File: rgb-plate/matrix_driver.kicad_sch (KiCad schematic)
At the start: 0 parts

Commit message: added additional sheets and leds with matrix driver and first regulator
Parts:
- added R1: R, symbol Device:R
- added R2: 10k, symbol Device:R
- added U1: LP5891MRRFR, VQFN76_RRF_TEX, symbol ul_LP5891MRRFR:LP5891MRRFR
- added U2: TPS562202, Package_TO_SOT_SMD:SOT-563, symbol Regulator_Switching:TPS562202
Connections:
- new net: R2.2, U2.5 (EN)
- new net: R1.1, U1.20 (IREF)
- new net +12V: R2.1, U2.1 (VIN)
- new net +3V3: U1.8 (VCC)
- new net B0: U1.3 (B0), U1.6 (B1)
- new net B10: U1.36 (B10)
- new net B12: U1.42 (B12)
- new net B13: U1.45 (B13)
- new net B14: U1.52 (B14)
- new net B15: U1.55 (B15)
- new net B2: U1.13 (B2)
- new net B3: U1.16 (B3)
- new net B4: U1.19 (B4)
- new net B5: U1.23 (B5)
- new net B6: U1.26 (B6)
- new net B7: U1.29 (B7)
- new net B8: U1.30 (B8)
- new net B9: U1.33 (B9)
- new net G0: U1.2 (G0), U1.5 (G1)
- new net G10: U1.37 (G10)
- new net G11: U1.39 (B11), U1.40 (G11)
- new net G12: U1.43 (G12)
- new net G13: U1.46 (G13)
- new net G14: U1.53 (G14)
- new net G15: U1.56 (G15)
- new net G2: U1.12 (G2)
- new net G3: U1.15 (G3)
- new net G4: U1.18 (G4)
- new net G5: U1.22 (G5)
- new net G6: U1.25 (G6)
- new net G7: U1.28 (G7)
- new net G8: U1.31 (G8)
- new net G9: U1.34 (G9)
- new net GND: R1.2, U1.7 (GND), U1.77 (EPAD), U2.3 (GND)
- new net L0: U1.76 (LINE0)
- new net L1: U1.75 (LINE1)
- new net L10: U1.66 (LINE10)
- new net L11: U1.65 (LINE11)
- new net L12: U1.64 (LINE12)
- new net L13: U1.63 (LINE13)
- new net L14: U1.62 (LINE14)
- new net L15: U1.61 (LINE15)
- new net L2: U1.74 (LINE2)
- new net L3: U1.73 (LINE3)
- new net L4: U1.72 (LINE4)
- new net L5: U1.71 (LINE5)
- new net L6: U1.70 (LINE6)
- new net L7: U1.69 (LINE7)
- new net L8: U1.68 (LINE8)
- new net L9: U1.67 (LINE9)
- new net R0: U1.1 (R0), U1.4 (R1)
- new net R10: U1.38 (R10)
- new net R11: U1.41 (R11)
- new net R12: U1.44 (R12)
- new net R13: U1.47 (R13)
- new net R14: U1.54 (R14)
- new net R15: U1.57 (R15)
- new net R2: U1.11 (R2)
- new net R3: U1.14 (R3)
- new net R4: U1.17 (R4)
- new net R5: U1.21 (R5)
- new net R6: U1.24 (R6)
- new net R7: U1.27 (R7)
- new net R8: U1.32 (R8)
- new net R9: U1.35 (R9)

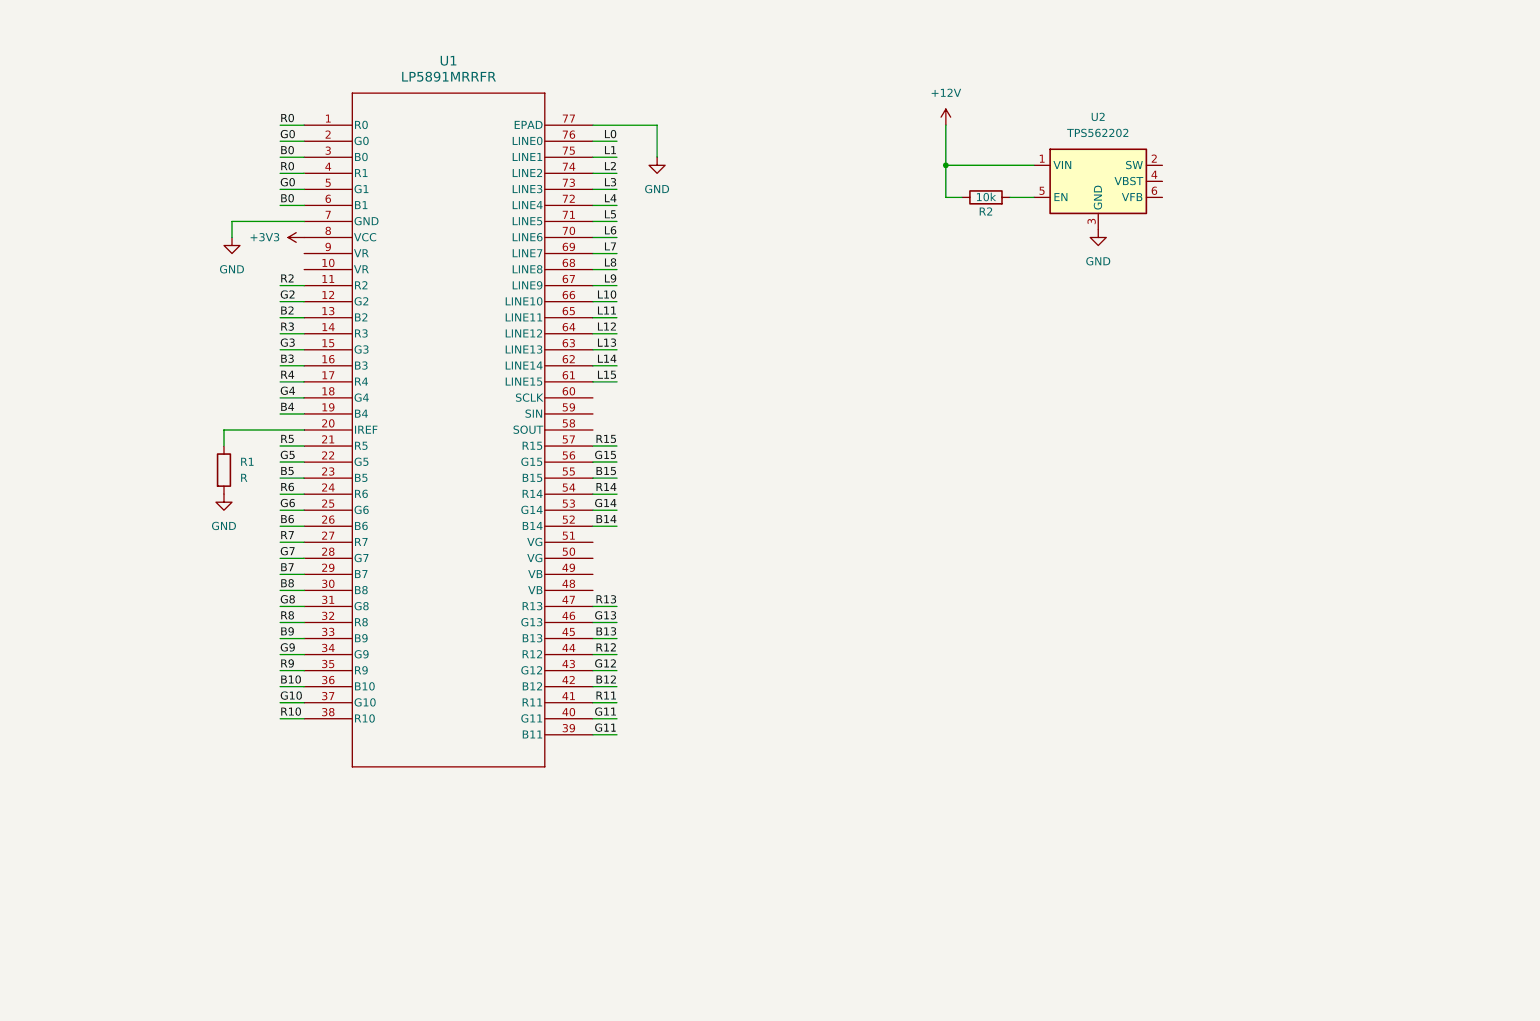
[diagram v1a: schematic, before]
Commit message: added 3 regulators for power stage
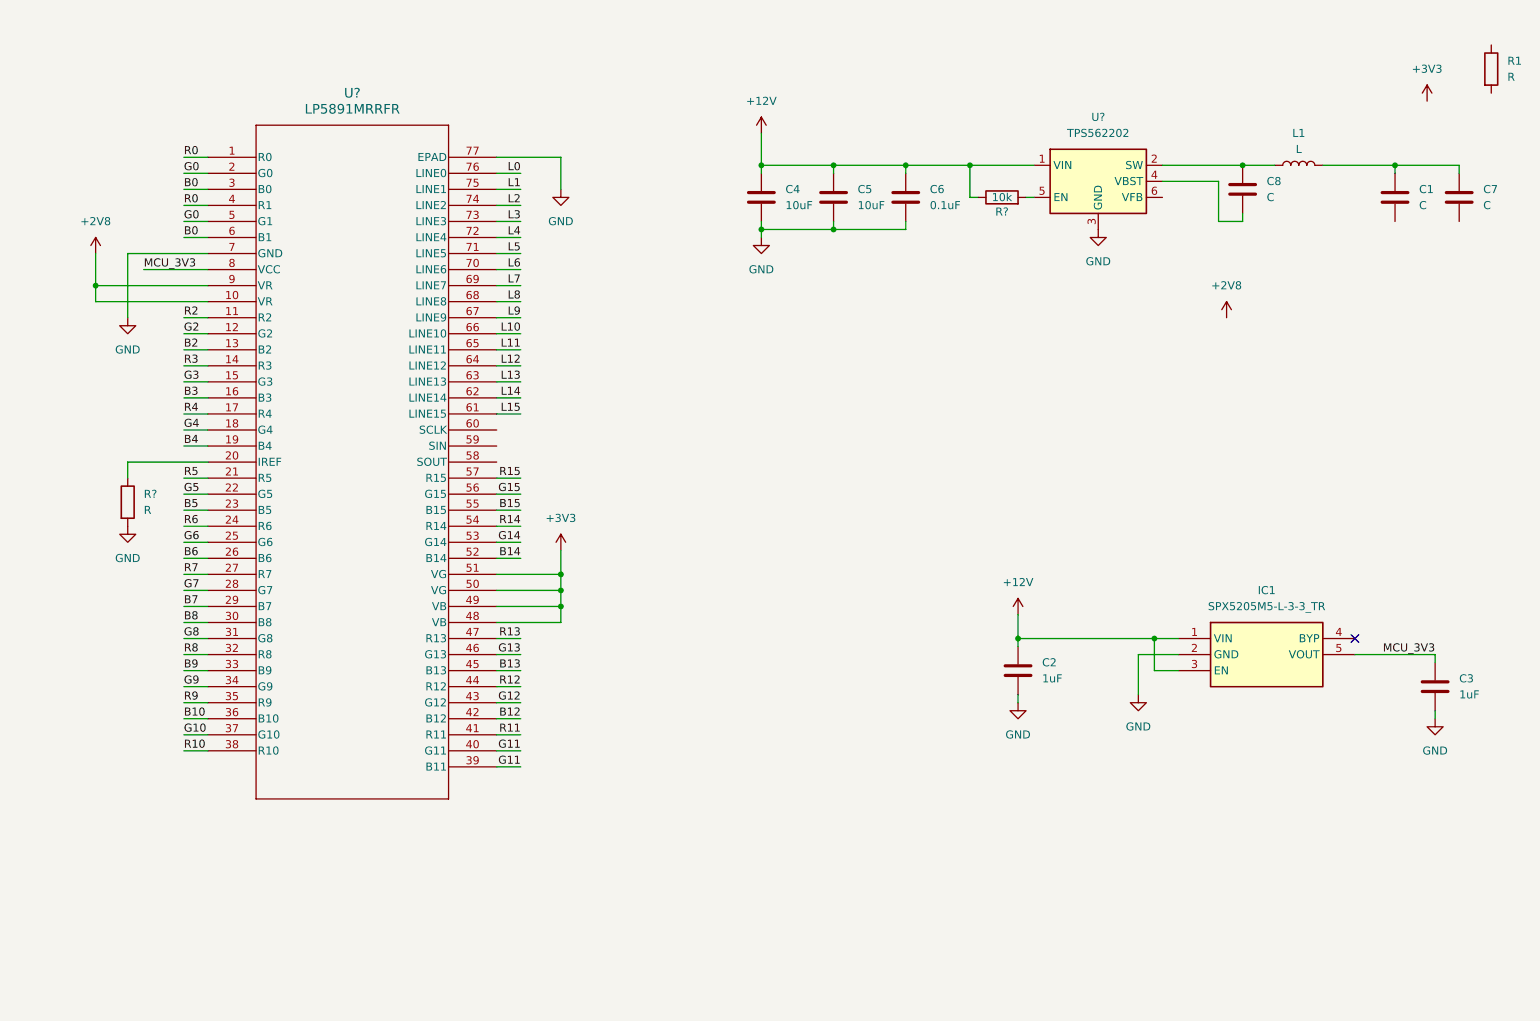
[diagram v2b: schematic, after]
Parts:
- added C1, C7, C8: C, symbol Device:C
- added C2, C3: 1uF, symbol Device:C
- added C4, C5: 10uF, symbol Device:C
- added C6: 0.1uF, symbol Device:C
- added IC1: SPX5205M5-L-3-3_TR, SOT95P280X145-5N, symbol SPX5205M5-L-3-3_TR:SPX5205M5-L-3-3_TR
- added L1: L, symbol Device:L
- added R1: R, symbol Device:R
- renumbered R2 to R?, R1 to R?, U2 to U?, U1 to U?
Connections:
- net +12V: now also C2.1, C4.1, C5.1, C6.1, IC1.1 (VIN), IC1.3 (EN)
- net +3V3: now also U?.48 (VB), U?.49 (VB), U?.50 (VG), U?.51 (VG); no longer U?.8 (VCC)
- net GND: now also C2.2, C3.2, C4.2, C5.2, C6.2, IC1.2 (GND)
- net at U?.2 (SW): now also C8.1, L1.1
- net at U?.4 (VBST): now also C8.2
- net +2V8: now reaches U?.10 (VR)
- net +2V8: now also U?.9 (VR)
- new net: C1.2, C7.2, L1.2
- new net MCU_3V3: C3.1, IC1.5 (VOUT), U?.8 (VCC)
- no-connect marks 0 -> 1
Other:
- moved on the sheet: R?, U?

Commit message: added regulators and components
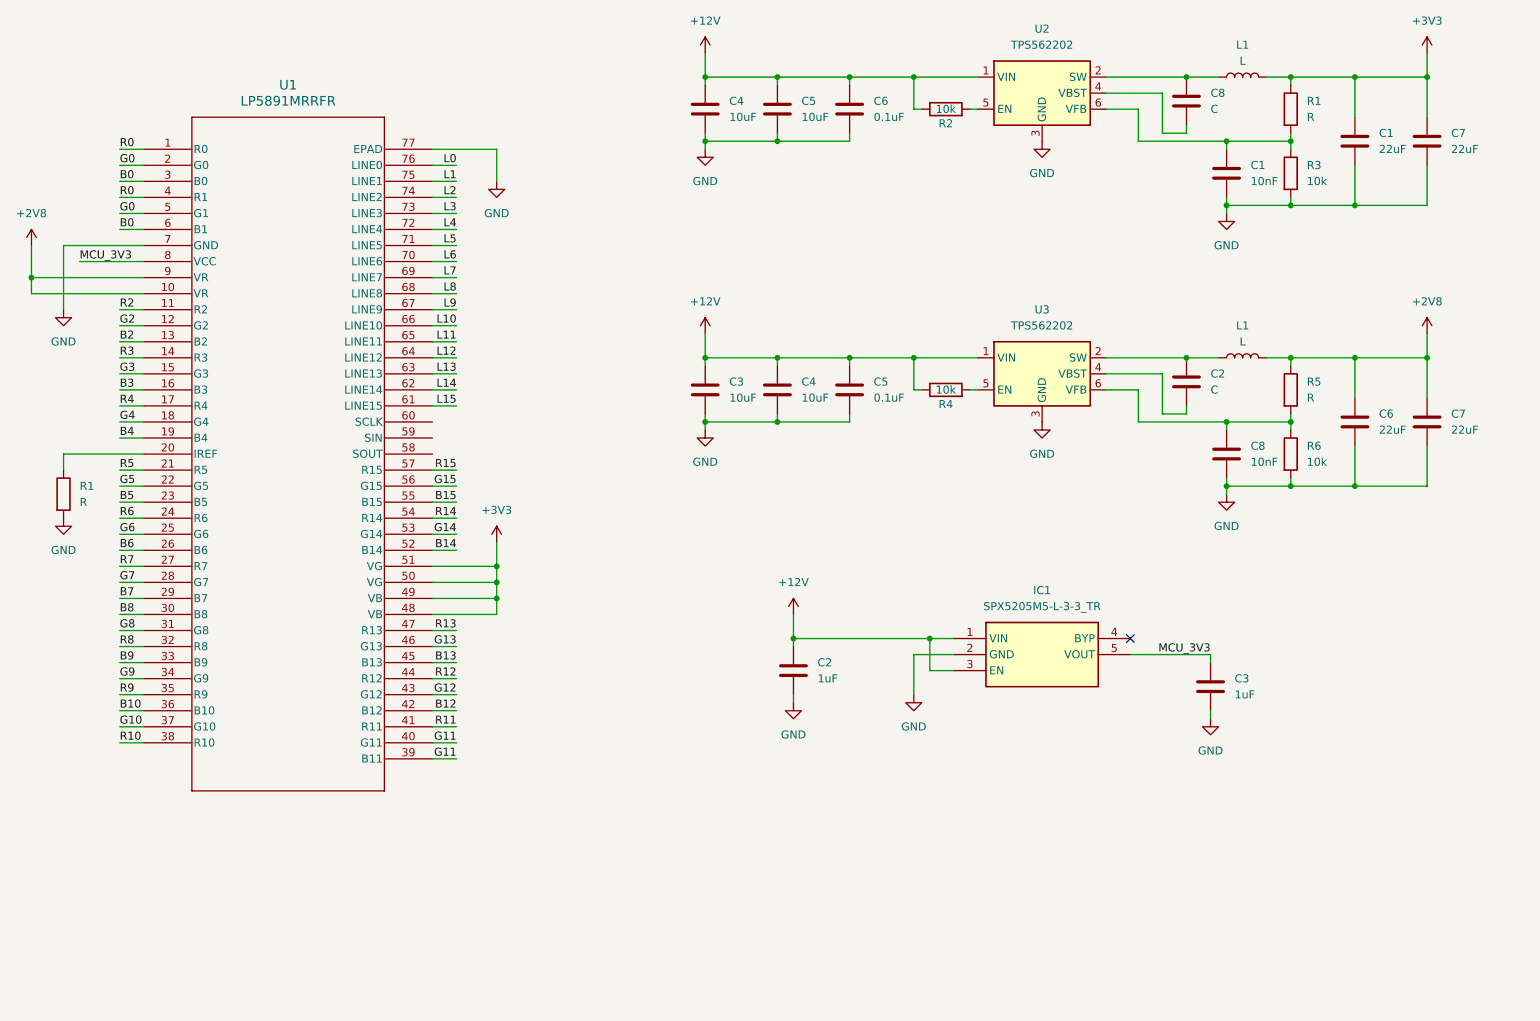
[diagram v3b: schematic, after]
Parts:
- added C1, C8: 10nF, symbol Device:C
- added C2: C, symbol Device:C
- added C3, C4: 10uF, symbol Device:C
- added C5: 0.1uF, symbol Device:C
- added C6, C7: 22uF, symbol Device:C
- added L1: L, symbol Device:L
- added R3, R4, R6: 10k, symbol Device:R
- added R5: R, symbol Device:R
- added U3: TPS562202, Package_TO_SOT_SMD:SOT-563, symbol Regulator_Switching:TPS562202
- C1, C7: value C -> 22uF
- gave numbers to parts that had none: 4
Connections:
- net +12V: now also C3.1, C4.1, C5.1, R4.1, U3.1 (VIN)
- net +2V8: now also C6.2, C7.2, L1.2, R5.1
- net +3V3: now also C1.2, C7.2, L1.2, R1.1
- net GND: now also C1.1, C7.1, C1.1, C3.2, C4.2, C5.2, C6.1, C7.1, C8.1, R3.2, R6.2, U3.3 (GND)
- net at R1.2: now also U2.6 (VFB), C1.2, R3.1
- new net: C8.2, R5.2, R6.1, U3.6 (VFB)
- new net: R4.2, U3.5 (EN)
- new net: C2.1, L1.1, U3.2 (SW)
- new net: C2.2, U3.4 (VBST)
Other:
- moved on the sheet: C1, C2, C3, C4, C5, C6, C7, C8, IC1, L1, R1, R2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

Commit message: initial layout on single board, may need to split up
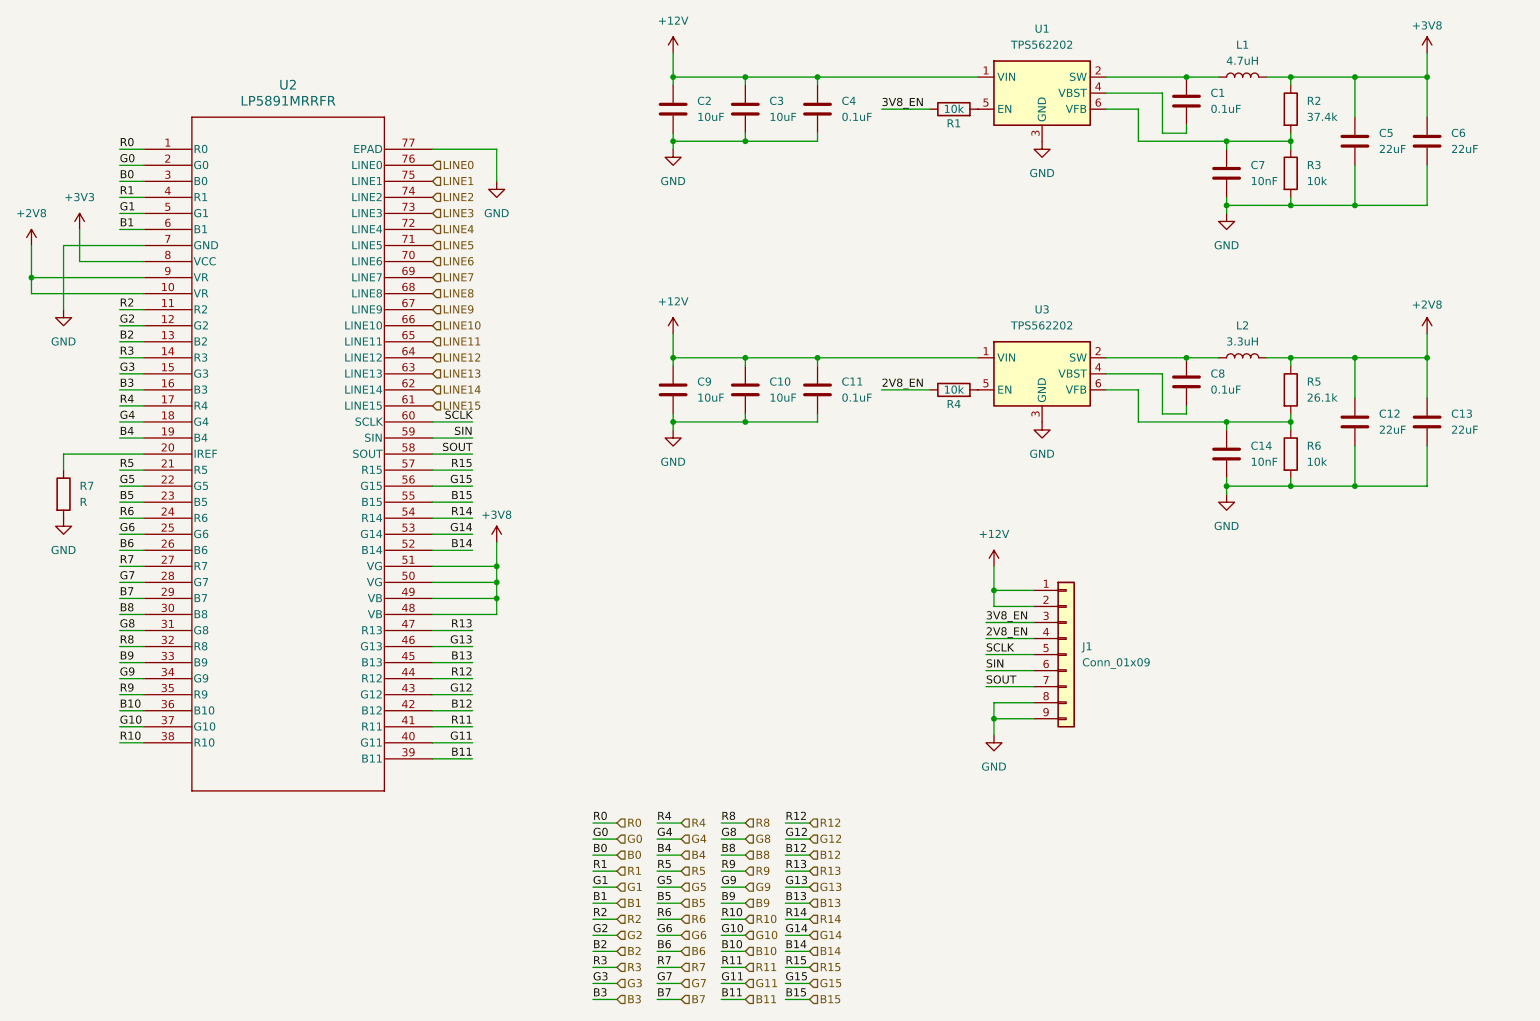
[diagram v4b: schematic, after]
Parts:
- removed C2, C3: 1uF, symbol Device:C
- removed IC1: SPX5205M5-L-3-3_TR, SOT95P280X145-5N, symbol SPX5205M5-L-3-3_TR:SPX5205M5-L-3-3_TR
- added J1: Conn_01x09, symbol Connector_Generic:Conn_01x09
- C1: renamed from C8; value C -> 0.1uF; footprint (none) -> Capacitor_SMD:C_0603_1608Metric
- C10, C2: renamed from C4; footprint (none) -> Capacitor_SMD:C_1206_3216Metric
- C11: renamed from C5; footprint (none) -> Capacitor_SMD:C_0603_1608Metric
- C12: renamed from C6; footprint (none) -> Capacitor_SMD:C_1206_3216Metric
- C13, C6: renamed from C7; footprint (none) -> Capacitor_SMD:C_1206_3216Metric
- C14: renamed from C8; footprint (none) -> Capacitor_SMD:C_0603_1608Metric
- C3: renamed from C5; footprint (none) -> Capacitor_SMD:C_1206_3216Metric
- C4: renamed from C6; footprint (none) -> Capacitor_SMD:C_0603_1608Metric
- C5: renamed from C1; footprint (none) -> Capacitor_SMD:C_1206_3216Metric
- C7: renamed from C1; footprint (none) -> Capacitor_SMD:C_0603_1608Metric
- C8: renamed from C2; value C -> 0.1uF; footprint (none) -> Capacitor_SMD:C_0603_1608Metric
- C9: renamed from C3; footprint (none) -> Capacitor_SMD:C_1206_3216Metric
- L1: value L -> 4.7uH
- L2: renamed from L1; value L -> 3.3uH
- R1: renamed from R2; footprint (none) -> Resistor_SMD:R_0603_1608Metric
- R2: renamed from R1; value R -> 37.4k; footprint (none) -> Resistor_SMD:R_0603_1608Metric
- R3, R4, R6: footprint (none) -> Resistor_SMD:R_0603_1608Metric
- R5: value R -> 26.1k; footprint (none) -> Resistor_SMD:R_0603_1608Metric
- R7: renamed from R1; footprint (none) -> Resistor_SMD:R_0603_1608Metric
- U2: renamed from U1; footprint VQFN76_RRF_TEX -> ul_LP5891MRRFR:VQFN76_RRF_TEX
- renumbered U2 to U1
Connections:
- net MCU_3V3 is gone; now on net +3V3: U2.8 (VCC)
- net +12V: now also J1.1 (Pin_1), J1.2 (Pin_2); no longer R1.1, R4.1
- net +3V3: no longer C5.2, C6.2, L1.2, R2.1, U2.48 (VB), U2.49 (VB), U2.50 (VG), U2.51 (VG)
- net B0: no longer U2.6 (B1)
- net G0: no longer U2.5 (G1)
- net G11: no longer U2.39 (B11)
- net GND: now also J1.8 (Pin_8), J1.9 (Pin_9)
- net R0: no longer U2.4 (R1)
- net SOUT: now reaches U2.58 (SOUT)
- net SOUT: now also J1.7 (Pin_7)
- net SIN: now reaches U2.59 (SIN)
- net SIN: now also J1.6 (Pin_6)
- net SCLK: now reaches U2.60 (SCLK)
- net SCLK: now also J1.5 (Pin_5)
- net L0 renamed LINE0
- net L1 renamed LINE1
- net L10 renamed LINE10
- net L11 renamed LINE11
- net L12 renamed LINE12
- net L13 renamed LINE13
- net L14 renamed LINE14
- net L15 renamed LINE15
- net L2 renamed LINE2
- net L3 renamed LINE3
- net L4 renamed LINE4
- net L5 renamed LINE5
- net L6 renamed LINE6
- net L7 renamed LINE7
- net L8 renamed LINE8
- net L9 renamed LINE9
- new net +3V8: C5.2, C6.2, L1.2, R2.1, U2.48 (VB), U2.49 (VB), U2.50 (VG), U2.51 (VG)
- new net 2V8_EN: J1.4 (Pin_4), R4.1
- new net 3V8_EN: J1.3 (Pin_3), R1.1
- new net B1: U2.6 (B1)
- new net B11: U2.39 (B11)
- new net G1: U2.5 (G1)
- new net R1: U2.4 (R1)
- no-connect marks 1 -> 0
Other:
- moved on the sheet: C10, C11, C2, C3, C4, C9, R1, R4
